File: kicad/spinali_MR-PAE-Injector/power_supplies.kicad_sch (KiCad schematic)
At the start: 63 parts, among them J1 5055780421, J13 5055780421, Q1 BUK6D56-60EX, Q2 BUK6D56-60EX, U1 LM74700, U16 LM74700, U2 NX5P3363UKZ, U3 LM5160DNTJ, U4 NX5P3363UKZ, U5 MIC5504-1.8YMT, U6 MPM3811GG-Z

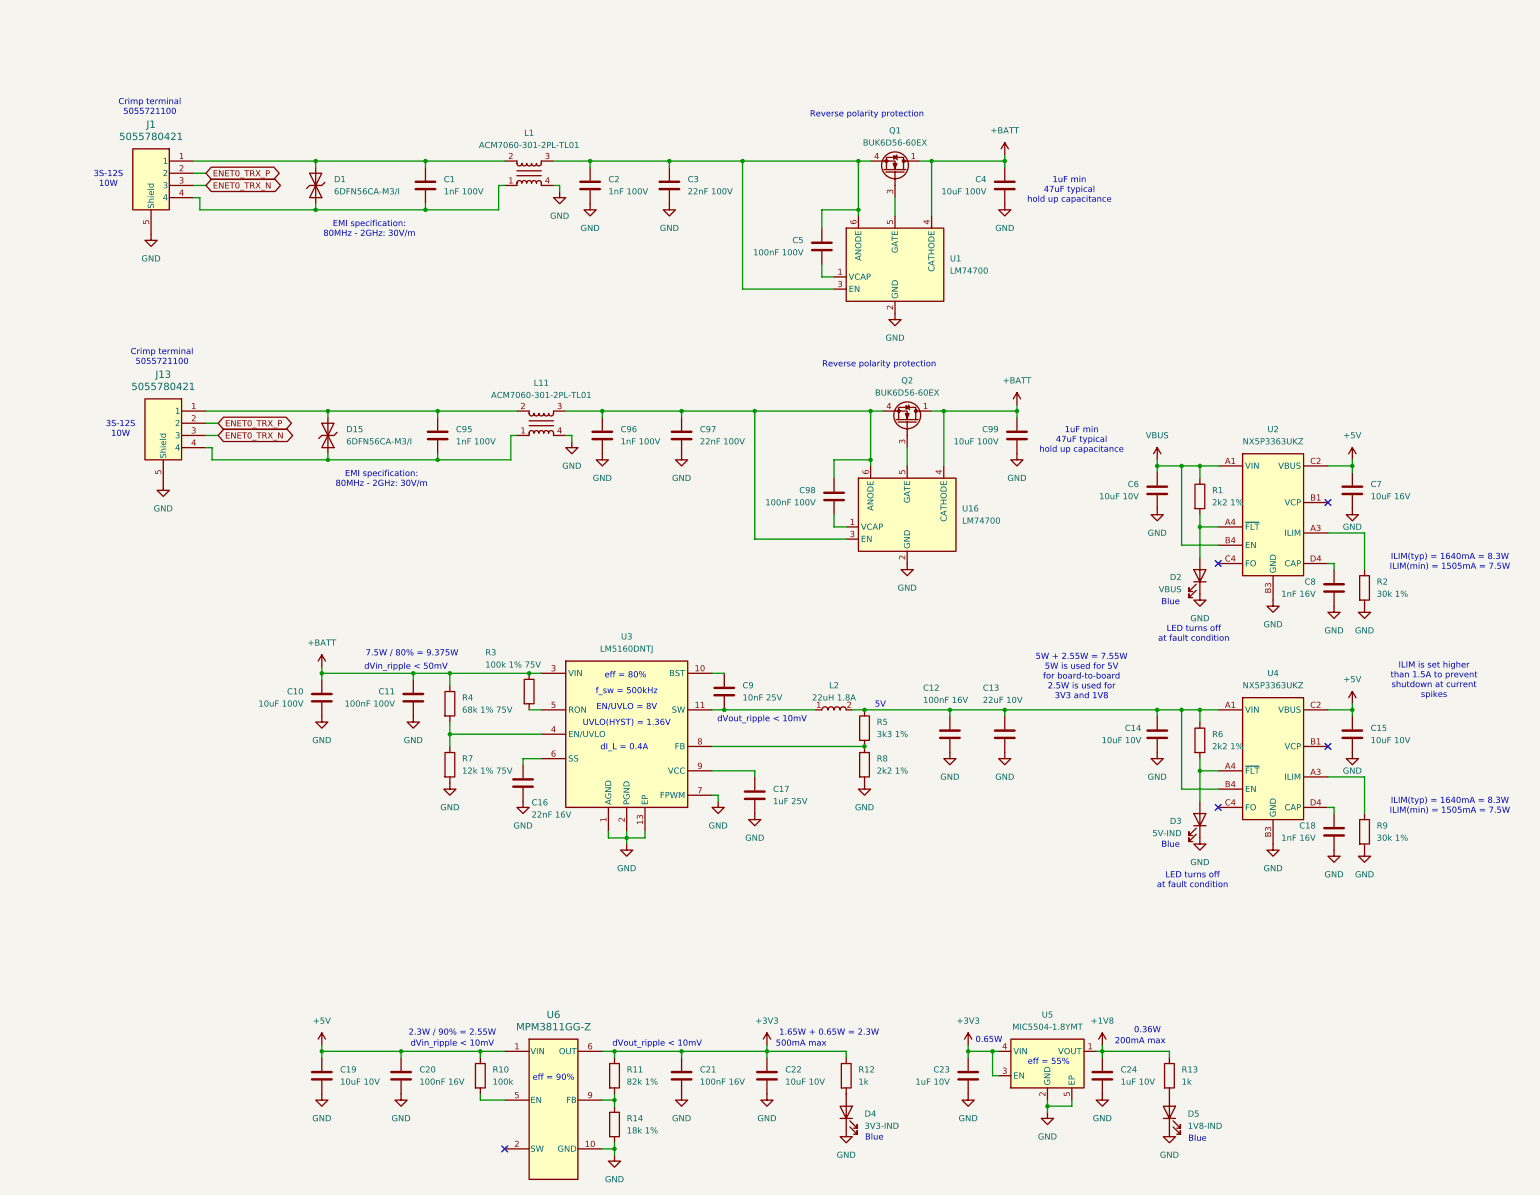
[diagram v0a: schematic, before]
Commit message: Draft design work
Cutting original schematics to basics.
Questions aroung the LM5160 regulator
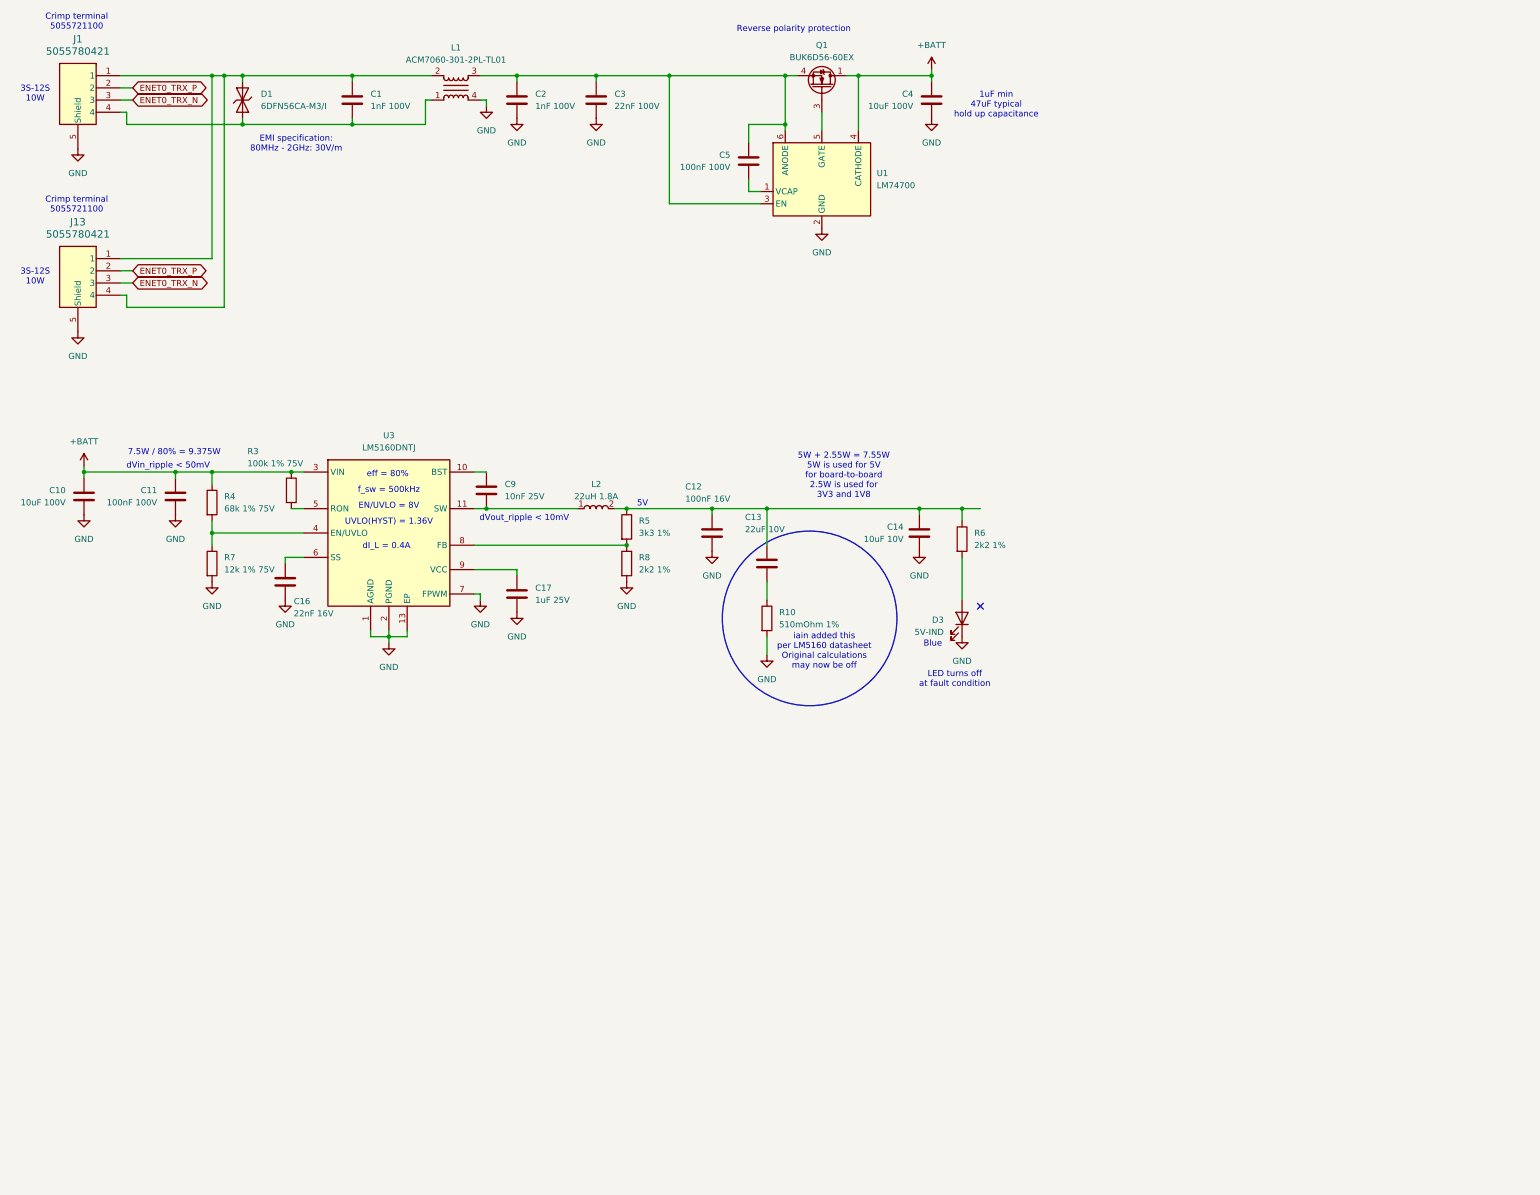
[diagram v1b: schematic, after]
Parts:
- removed C15, C19, C22, C6: 10uF 10V, Capacitor_SMD:C_0805_2012Metric, symbol Device:C
- removed C18, C8: 1nF 16V, Capacitor_SMD:C_0402_1005Metric, symbol Device:C
- removed C20, C21: 100nF 16V, Capacitor_SMD:C_0402_1005Metric, symbol Device:C
- removed C23, C24: 1uF 10V, Capacitor_SMD:C_0402_1005Metric, symbol Device:C
- removed C7: 10uF 16V, Capacitor_SMD:C_0805_2012Metric, symbol Device:C
- removed C95, C96: 1nF 100V, Capacitor_SMD:C_0402_1005Metric, symbol Capacitors:GRM1885C2A102JA01D
- removed C97: 22nF 100V, Capacitor_SMD:C_0603_1608Metric, symbol Device:C
- removed C98: 100nF 100V, Capacitor_SMD:C_0603_1608Metric, symbol Device:C
- removed C99: 10uF 100V, Capacitor_SMD:C_1210_3225Metric, symbol Device:C
- removed D15: 6DFN56CA-M3/I, Diodes:DFN3820A, symbol Diodes:TVS-Bi,SMAJ43CA
- removed D2: VBUS, LED_SMD:LED_0402_1005Metric, symbol Device:LED
- removed D4: 3V3-IND, LED_SMD:LED_0402_1005Metric, symbol Device:LED
- removed D5: 1V8-IND, LED_SMD:LED_0402_1005Metric, symbol Device:LED
- removed L11: ACM7060-301-2PL-TL01, Inductors:ACM70603012PLTL01, symbol Inductors:ACM7060-301-2PL-TL01
- removed Q2: BUK6D56-60EX, MOSFETs:BUK6D5660EX, symbol MOSFETs:BUK6D56-60EX
- removed R1: 2k2 1%, Resistor_SMD:R_0402_1005Metric, symbol Device:R
- removed R11: 82k 1%, Resistor_SMD:R_0402_1005Metric, symbol Device:R
- removed R12, R13: 1k, Resistor_SMD:R_0402_1005Metric, symbol Device:R
- removed R14: 18k 1%, Resistor_SMD:R_0402_1005Metric, symbol Device:R
- removed R2, R9: 30k 1%, Resistor_SMD:R_0402_1005Metric, symbol Device:R
- removed U16: LM74700, Package_TO_SOT_SMD:SOT-23-6, symbol Power_Management:LM74700
- removed U2, U4: NX5P3363UKZ, NXP_BGA:BGA16C50P4X4_220X220X60, symbol Power:NX5P3363UKZ
- removed U5: MIC5504-1.8YMT, Power:VREG_MIC5504-3.3YMT-TZ, symbol Power:MIC5504-1.8YMT
- removed U6: MPM3811GG-Z, Power:QFN2x2x1p6_MPM3811_MNP, symbol Power:MPM3811GG-Z
- R10: value 100k -> 510mOhm 1%; DigiKey 13-RC0402FR-7W100KLCT-ND -> YAG3467CT-ND; JLCPCB C606167 -> C144773; MFPN RC0402FR-7W100KL -> AC0402FR-072K2L
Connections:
- net GND: now also R10.2; no longer C13.1
- net at J13.1: now also C1.1, D1.2, J1.1, J13.4, L1.2
- net +5V: no longer names the net of R10.1
- net +5V: now also C13.1
- no-connect marks 5 -> 1
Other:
- note added: "iain added this per LM5160 datasheet Original calculations may now be off"
- note removed: "0.36W"
- note removed: "0.65W"
- note removed: "1.65W + 0.65W = 2.3W"
- note removed: "2.3W / 90% = 2.55W"
- note removed: "200mA max"
- note removed: "500mA max"
- note removed: "ILIM is set higher than 1.5A to prevent shutdown at current spikes"
- note removed: "ILIM(typ) = 1640mA = 8.3W ILIM(min) = 1505mA = 7.5W"
- note removed: "dVin_ripple < 10mV"
- note removed: "eff = 55%"
- note removed: "eff = 90%"
- moved on the sheet: C1, C10, C11, C12, C13, C14, C16, C17, C2, C3, C4, C5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
